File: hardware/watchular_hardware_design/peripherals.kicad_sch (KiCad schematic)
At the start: 45 parts, among them Q1 BSS123, Q2 BSS123, Q3 BSS123, Q4 BSS123

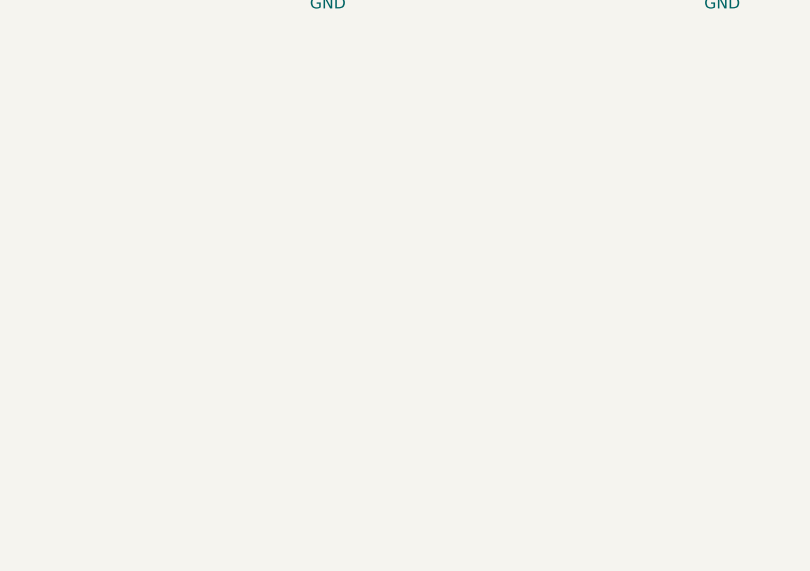
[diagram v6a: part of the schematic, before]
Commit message: Added a 16 position header.
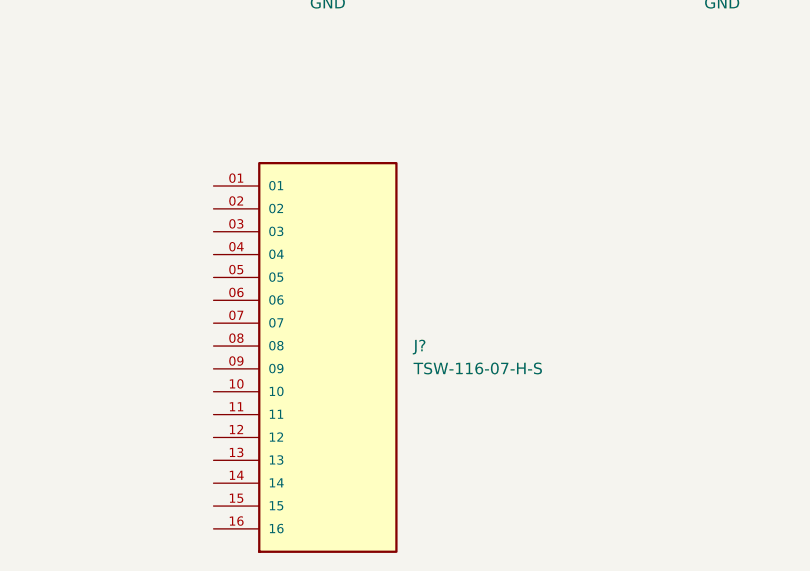
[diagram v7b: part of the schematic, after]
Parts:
- added J?: TSW-116-07-H-S, SAMTEC_TSW-116-07-H-S, symbol TSW-116-07-H-S:TSW-116-07-H-S
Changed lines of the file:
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@@
   (title_block
     (title "Peripherals for the watch")
-    (date "2022-06-16")
+    (date "2022-06-29")
     (rev "v0.1")
     (company "Lilordag")
@@
     (pin "2")
   )
+  (symbol (lib_id "TSW-116-07-H-S:TSW-116-07-H-S") (at 136.525 133.35 0) (unit 1)
+    (in_bom yes) (on_board yes) (fields_autoplaced)
+    (property "Reference" "J?" (id 0) (at 146.05 130.8099 0)
+      (effects (font (size 1.27 1.27)) (justify left))
+    )
+    (property "Value" "TSW-116-07-H-S" (id 1) (at 146.05 133.3499 0)
+      (effects (font (size 1.27 1.27)) (justify left))
+    )
+    (property "Footprint" "SAMTEC_TSW-116-07-H-S" (id 2) (at 136.525 133.35 0)
+      (effects (font (size 1.27 1.27)) (justify left bottom) hide)
+    )
+    (property "Datasheet" "" (id 3) (at 136.525 133.35 0)
+      (effects (font (size 1.27 1.27)) (justify left bottom) hide)
+    )
+    (property "STANDARD" "Manufacturer Recommendations" (id 4) (at 136.525 133.35 0)
+      (effects (font (size 1.27 1.27)) (justify left bottom) hide)
+    )
+    (property "MANUFACTURER" "Samtec" (id 5) (at 136.525 133.35 0)
+      (effects (font (size 1.27 1.27)) (justify left bottom) hide)
+    )
+    (property "PARTREV" "R" (id 6) (at 136.525 133.35 0)
+      (effects (font (size 1.27 1.27)) (justify left bottom) hide)
+    )
+    (pin "01")
+    (pin "02")
+    (pin "03")
+    (pin "04")
+    (pin "05")
+    (pin "06")
+    (pin "07")
+    (pin "08")
+    (pin "09")
+    (pin "10")
+    (pin "11")
+    (pin "12")
+    (pin "13")
+    (pin "14")
+    (pin "15")
+    (pin "16")
+  )
   (symbol (lib_id "Device:LED") (at 216.535 36.195 180) (unit 1)

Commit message: Added 15 position 2.45mm headers.
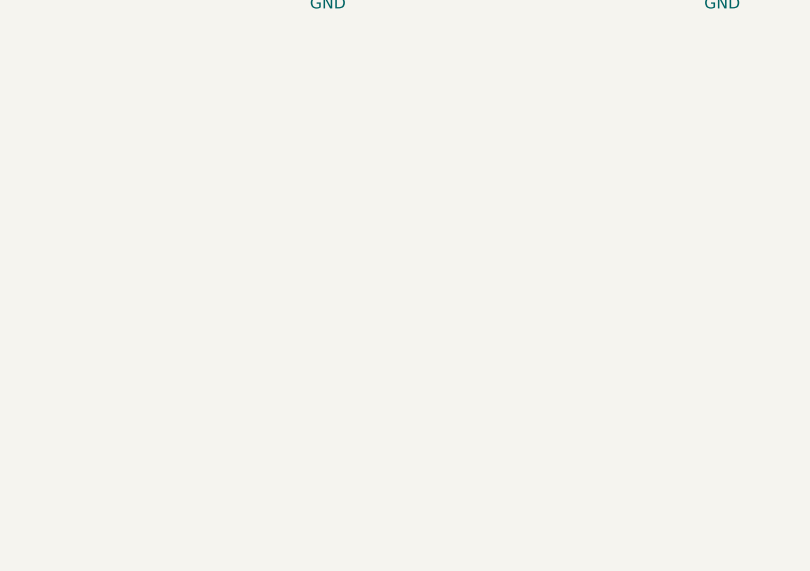
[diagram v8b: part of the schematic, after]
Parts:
- removed J?: TSW-116-07-H-S, SAMTEC_TSW-116-07-H-S, symbol TSW-116-07-H-S:TSW-116-07-H-S
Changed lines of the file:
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@@
   (symbol (lib_id "power:GND") (at 38.735 122.555 0) (unit 1)
     (in_bom yes) (on_board yes) (fields_autoplaced)
-    (property "Reference" "#PWR0101" (id 0) (at 38.735 128.905 0)
+    (property "Reference" "#PWR029" (id 0) (at 38.735 128.905 0)
       (effects (font (size 1.27 1.27)) hide)
     )
@@
   (symbol (lib_id "power:GND") (at 90.17 88.265 0) (unit 1)
     (in_bom yes) (on_board yes) (fields_autoplaced)
-    (property "Reference" "#PWR029" (id 0) (at 90.17 94.615 0)
+    (property "Reference" "#PWR031" (id 0) (at 90.17 94.615 0)
       (effects (font (size 1.27 1.27)) hide)
     )
@@
   (symbol (lib_id "power:GND") (at 136.525 88.265 0) (unit 1)
     (in_bom yes) (on_board yes) (fields_autoplaced)
-    (property "Reference" "#PWR030" (id 0) (at 136.525 94.615 0)
+    (property "Reference" "#PWR032" (id 0) (at 136.525 94.615 0)
       (effects (font (size 1.27 1.27)) hide)
     )
@@
   (symbol (lib_id "power:GND") (at 39.37 140.97 0) (unit 1)
     (in_bom yes) (on_board yes) (fields_autoplaced)
-    (property "Reference" "#PWR0102" (id 0) (at 39.37 147.32 0)
+    (property "Reference" "#PWR030" (id 0) (at 39.37 147.32 0)
       (effects (font (size 1.27 1.27)) hide)
     )
@@
   (symbol (lib_id "power:GND") (at 180.34 88.265 0) (unit 1)
     (in_bom yes) (on_board yes) (fields_autoplaced)
-    (property "Reference" "#PWR031" (id 0) (at 180.34 94.615 0)
+    (property "Reference" "#PWR033" (id 0) (at 180.34 94.615 0)
       (effects (font (size 1.27 1.27)) hide)
     )
@@
     (pin "2")
   )
-  (symbol (lib_id "TSW-116-07-H-S:TSW-116-07-H-S") (at 136.525 133.35 0) (unit 1)
-    (in_bom yes) (on_board yes) (fields_autoplaced)
-    (property "Reference" "J?" (id 0) (at 146.05 130.8099 0)
-      (effects (font (size 1.27 1.27)) (justify left))
-    )
-    (property "Value" "TSW-116-07-H-S" (id 1) (at 146.05 133.3499 0)
-      (effects (font (size 1.27 1.27)) (justify left))
-    )
-    (property "Footprint" "SAMTEC_TSW-116-07-H-S" (id 2) (at 136.525 133.35 0)
-      (effects (font (size 1.27 1.27)) (justify left bottom) hide)
-    )
-    (property "Datasheet" "" (id 3) (at 136.525 133.35 0)
-      (effects (font (size 1.27 1.27)) (justify left bottom) hide)
-    )
-    (property "STANDARD" "Manufacturer Recommendations" (id 4) (at 136.525 133.35 0)
-      (effects (font (size 1.27 1.27)) (justify left bottom) hide)
-    )
-    (property "MANUFACTURER" "Samtec" (id 5) (at 136.525 133.35 0)
-      (effects (font (size 1.27 1.27)) (justify left bottom) hide)
-    )
-    (property "PARTREV" "R" (id 6) (at 136.525 133.35 0)
-      (effects (font (size 1.27 1.27)) (justify left bottom) hide)
-    )
-    (pin "01")
-    (pin "02")
-    (pin "03")
-    (pin "04")
-    (pin "05")
-    (pin "06")
-    (pin "07")
-    (pin "08")
-    (pin "09")
-    (pin "10")
-    (pin "11")
-    (pin "12")
-    (pin "13")
-    (pin "14")
-    (pin "15")
-    (pin "16")
-  )
   (symbol (lib_id "Device:LED") (at 216.535 36.195 180) (unit 1)
     (in_bom yes) (on_board yes)
@@
   (symbol (lib_id "power:GND") (at 226.695 88.265 0) (unit 1)
     (in_bom yes) (on_board yes) (fields_autoplaced)
-    (property "Reference" "#PWR032" (id 0) (at 226.695 94.615 0)
-      (effects (font (size 1.27 1.27)) hide)
-    )
+    (property "Reference" "#PWR034" (id 0) (at 226.695 94.615 0)
+      (effects (font (size 1.27 1.27)) hide)
+    )
